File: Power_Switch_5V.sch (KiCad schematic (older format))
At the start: 7 parts

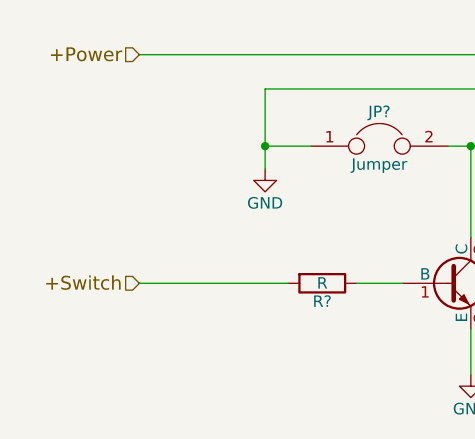
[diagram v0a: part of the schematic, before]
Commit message: rename '+Switch' to 'Switch'
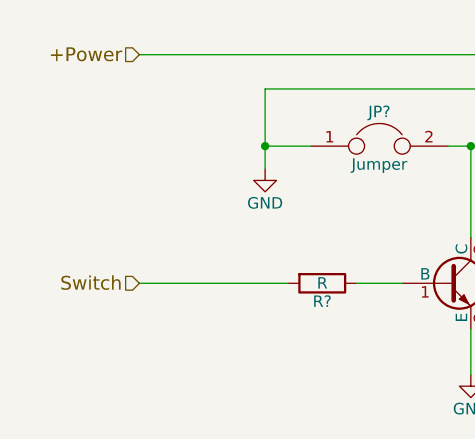
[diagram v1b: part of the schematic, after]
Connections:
- net +Switch renamed Switch
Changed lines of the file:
@@
 +Power
 Text HLabel 3350 4550 0    60   Input ~ 0
-+Switch
+Switch
 Wire Wire Line
 	3350 3550 4900 3550

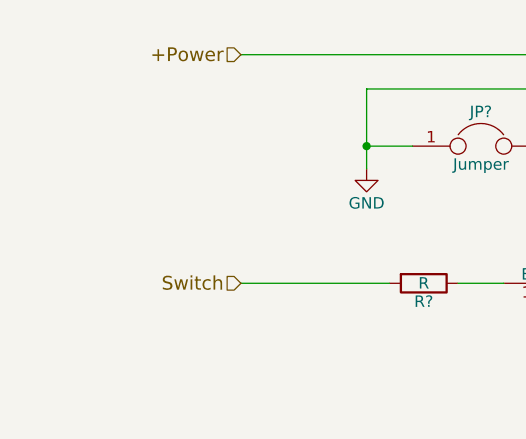
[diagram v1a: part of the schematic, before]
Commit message: change 'Switch' to 'Software_Switch'
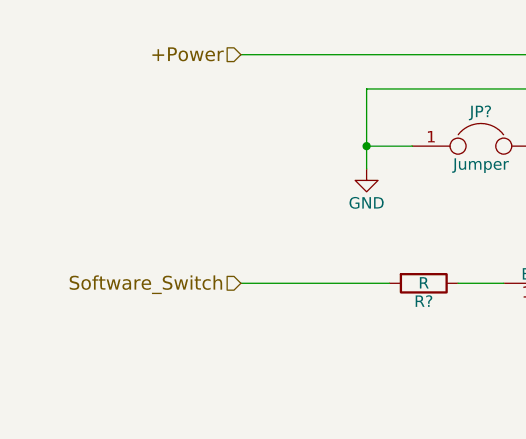
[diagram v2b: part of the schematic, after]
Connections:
- net Switch renamed Software_Switch
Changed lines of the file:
@@
 +Power
 Text HLabel 3350 4550 0    60   Input ~ 0
-Switch
+Software_Switch
 Wire Wire Line
 	3350 3550 4900 3550

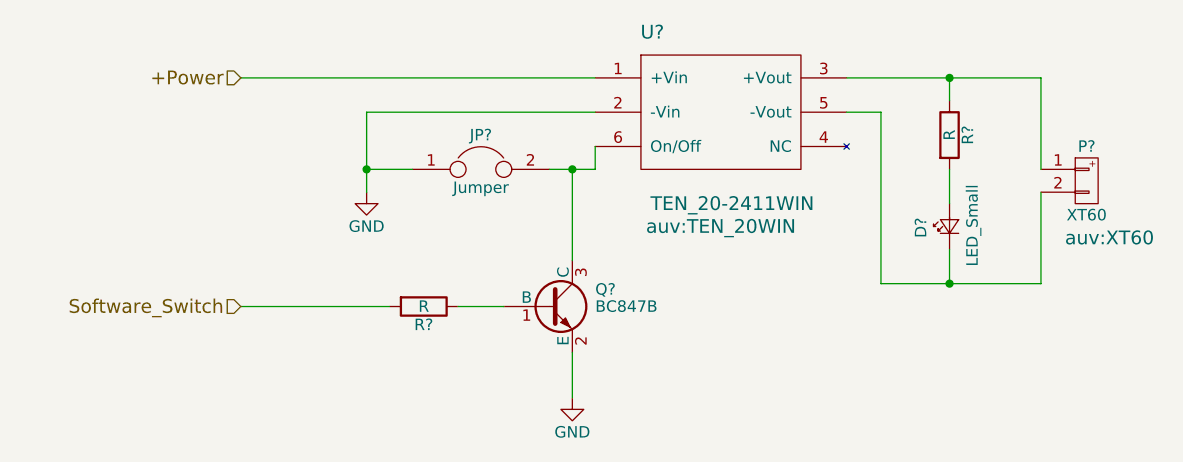
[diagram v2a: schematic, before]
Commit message: assign component value and change BC847B to BC817-40
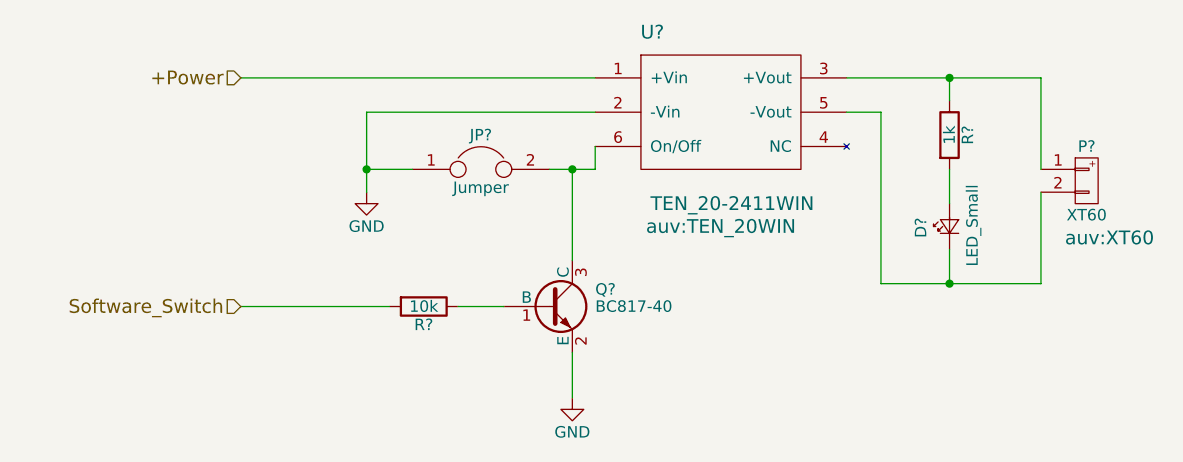
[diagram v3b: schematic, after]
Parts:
- removed Q?: BC847B, TO_SOT_Packages_SMD:SOT-23, symbol BC847B
- added Q?: BC817-40, TO_SOT_Packages_SMD:SOT-23, symbol BC817-40
- R?: value R -> 1k
- R?: value R -> 10k
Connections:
- net GND: now also Q?.2 (E)
- net at JP?.2, U?.6 (On/Off): now also Q?.3 (C)
- net at R?.1: now also Q?.1 (B)
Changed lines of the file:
@@
 P 6450 3800
 F 0 "R?" V 6530 3800 50  0000 C CNN
-F 1 "R" V 6450 3800 50  0000 C CNN
+F 1 "1k" V 6450 3800 50  0000 C CNN
 F 2 "Resistors_SMD:R_0603" V 6380 3800 50  0001 C CNN
 F 3 "" H 6450 3800 50  0001 C CNN
@@
 	1    0    0    -1
 $EndComp
-$Comp
-L BC847B Q?
-U 1 1 58DFDB54
-P 4700 4550
-F 0 "Q?" H 4900 4625 50  0000 L CNN
-F 1 "BC847B" H 4900 4550 50  0000 L CNN
-F 2 "TO_SOT_Packages_SMD:SOT-23" H 4900 4475 50  0001 L CIN
-F 3 "" H 4700 4550 50  0001 L CNN
-	1    4700 4550
-	1    0    0    -1
-$EndComp
 Wire Wire Line
 	4100 3950 3900 3950
@@
 P 4150 4550
 F 0 "R?" V 4230 4550 50  0000 C CNN
-F 1 "R" V 4150 4550 50  0000 C CNN
+F 1 "10k" V 4150 4550 50  0000 C CNN
 F 2 "Resistors_SMD:R_0603" V 4080 4550 50  0001 C CNN
 F 3 "" H 4150 4550 50  0001 C CNN
@@
 Wire Wire Line
 	4000 4550 3350 4550
+$Comp
+L BC817-40 Q?
+U 1 1 58E56AD9
+P 4700 4550
+F 0 "Q?" H 4900 4625 50  0000 L CNN
+F 1 "BC817-40" H 4900 4550 50  0000 L CNN
+F 2 "TO_SOT_Packages_SMD:SOT-23" H 4900 4475 50  0001 L CIN
+F 3 "" H 4700 4550 50  0001 L CNN
+	1    4700 4550
+	1    0    0    -1
+$EndComp
 $EndSCHEMATC
